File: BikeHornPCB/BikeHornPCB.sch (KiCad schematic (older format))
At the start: 20 parts, among them J1 Battery, J2 Horn, J3 Piezo, Q1 BC337, Q2 BC337

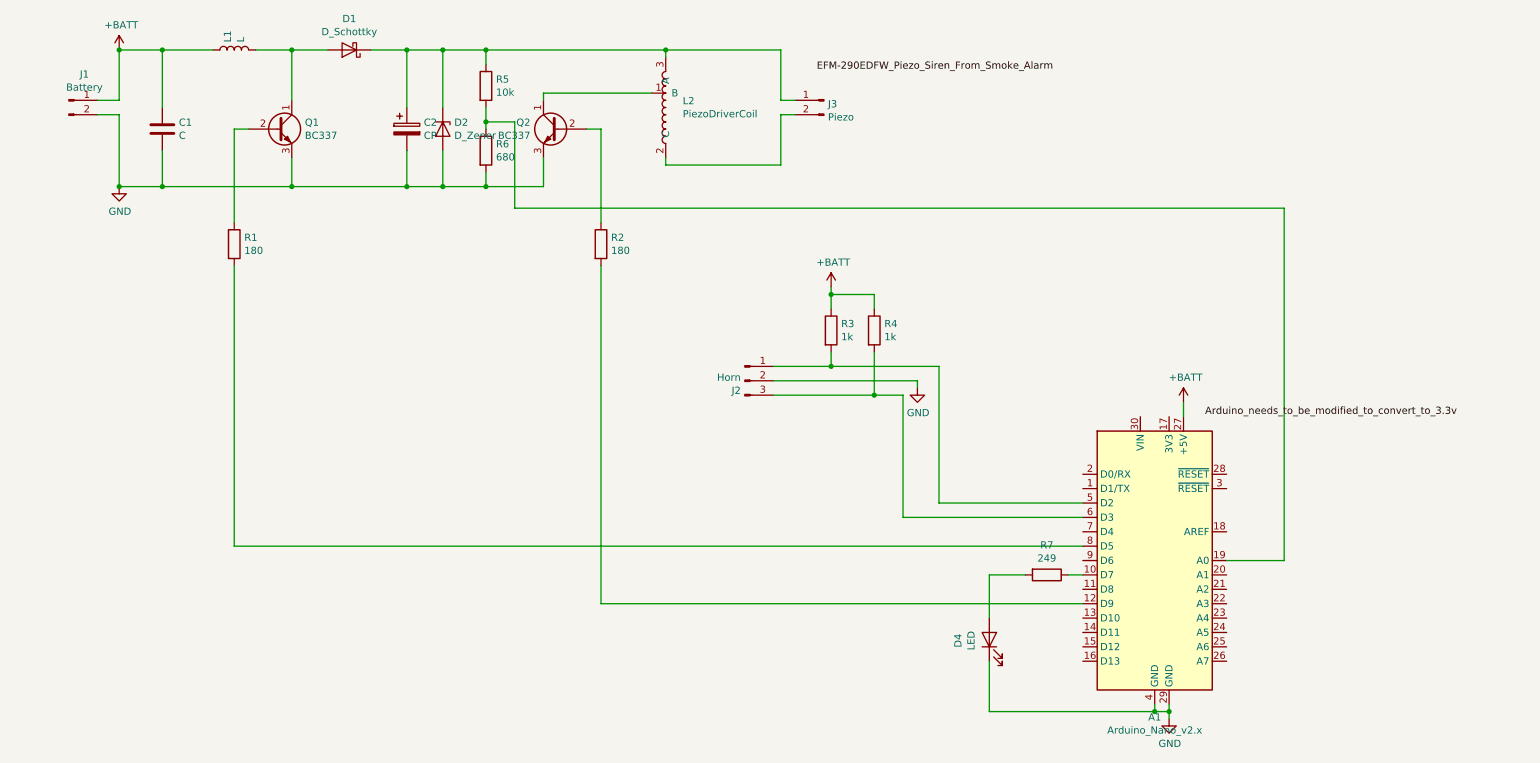
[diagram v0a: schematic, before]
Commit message: Added docs, runtime logging, revised PCB to fix issues from first version built
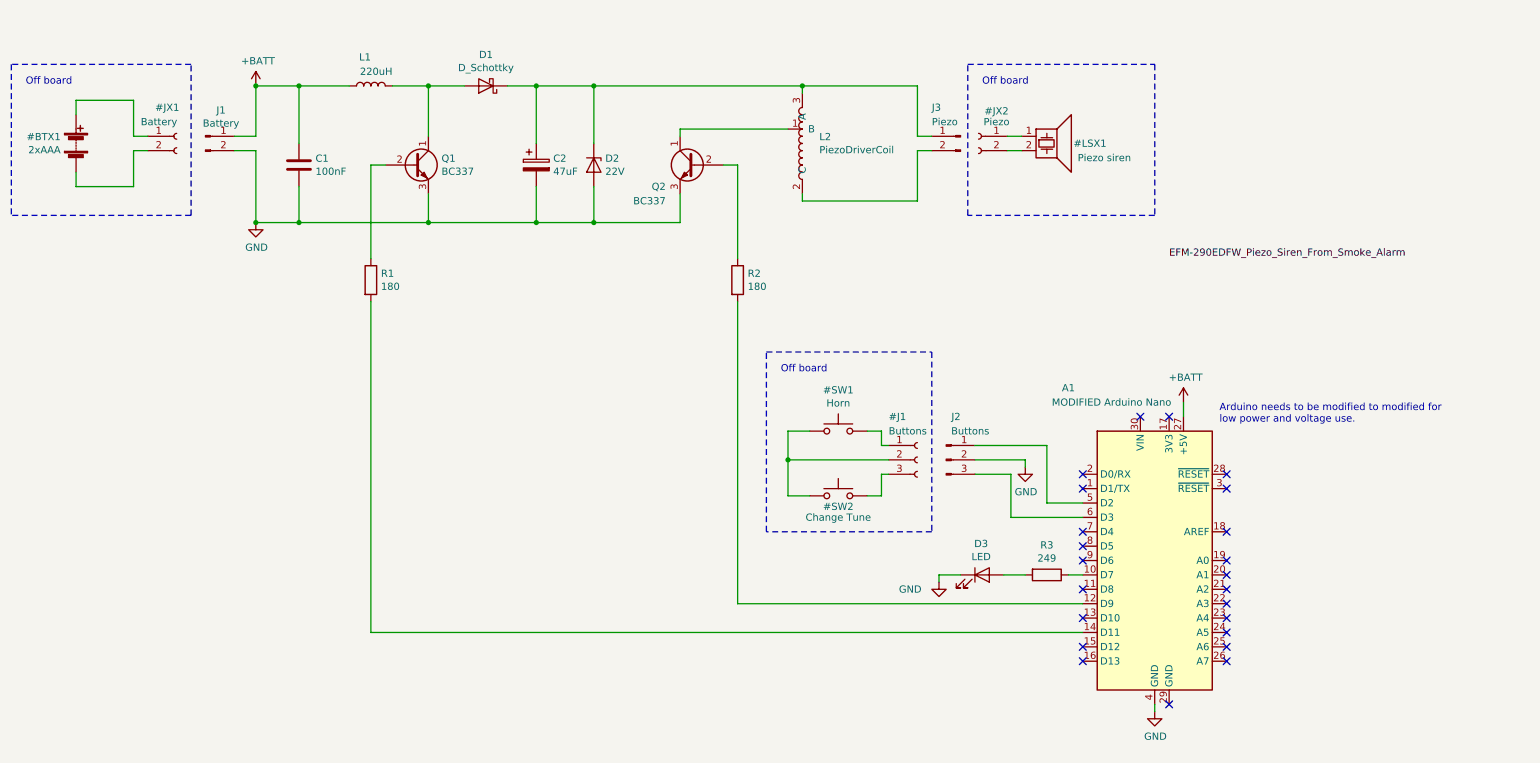
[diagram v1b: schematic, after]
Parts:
- removed R3, R4: 1k, Resistor_SMD:R_0805_2012Metric_Pad1.20x1.40mm_HandSolder, symbol Device:R
- removed R5: 10k, Resistor_SMD:R_0805_2012Metric_Pad1.20x1.40mm_HandSolder, symbol Device:R
- removed R6: 680, Resistor_SMD:R_0805_2012Metric_Pad1.20x1.40mm_HandSolder, symbol Device:R
- A1: value Arduino_Nano_v2.x -> MODIFIED Arduino Nano
- C1: value C -> 100nF
- C2: value CP -> 47uF
- D2: value D_Zener -> 22V
- J2: value Horn -> Buttons
- L1: value L -> 220uH
- renumbered D4 to D3, R7 to R3
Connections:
- net GND: no longer A1.29 (GND)
- net at A1.14 (D11): now also R1.2
- net at A1.8 (D5): no longer R1.2
- no-connect marks 0 -> 23
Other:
- note added: "Arduino needs to be modified to modified for\nlow power and voltage use."
- note added: "Off board"
- moved on the sheet: C1, C2, D1, D2, D3, J1, J2, J3, L1, L2, Q1, Q2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
